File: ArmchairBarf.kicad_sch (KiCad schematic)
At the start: 12 parts, among them J1 Conn_01x03_Socket, U1 WS2812-2020, U2 WS2812-2020, U3 WS2812-2020, U4 WS2812-2020, U5 WS2812-2020, U6 WS2812-2020, U7 WS2812-2020, U8 WS2812-2020, U9 WS2812-2020

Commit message: Cleaned up and made proper connections and repinned to hartk's suggestions
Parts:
- added C2, C3, C4: C, Capacitor_SMD:C_0402_1005Metric, symbol Device:C
- added J2: Conn_01x03_Socket, Connector_JST:JST_PH_B3B-PH-K_1x03_P2.00mm_Vertical, symbol Connector:Conn_01x03_Socket
- added U10, U11, U12: WS2812-2020, LED_WS2812-2020, symbol WS2812-2020:WS2812-2020
- J1: footprint (none) -> Connector_JST:JST_PH_B3B-PH-K_1x03_P2.00mm_Vertical
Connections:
- net at U9.1 (DO): now also U10.3 (DI)
- net GND: now reaches C1.2, U1.2 (GND), U2.2 (GND), U3.2 (GND), U4.2 (GND), U5.2 (GND), U6.2 (GND), U7.2 (GND), U8.2 (GND), U9.2 (GND)
- net GND: now also J1.2 (Pin_2), C2.2, C3.2, C4.2, J2.2 (Pin_2), U10.2 (GND), U11.2 (GND), U12.2 (GND); no longer J1.1 (Pin_1)
- net +5V: now reaches C1.1, J1.3 (Pin_3), U1.4 (VDD), U2.4 (VDD), U3.4 (VDD), U4.4 (VDD), U5.4 (VDD), U6.4 (VDD), U7.4 (VDD), U8.4 (VDD), U9.4 (VDD)
- net +5V: now also C2.1, C3.1, C4.1, J2.3 (Pin_3), U10.4 (VDD), U11.4 (VDD), U12.4 (VDD)
- net at R1.1: now also J1.1 (Pin_1); no longer J1.2 (Pin_2)
- new net: J2.1 (Pin_1), U12.1 (DO)
- new net: U10.1 (DO), U11.3 (DI)
- new net: U11.1 (DO), U12.3 (DI)

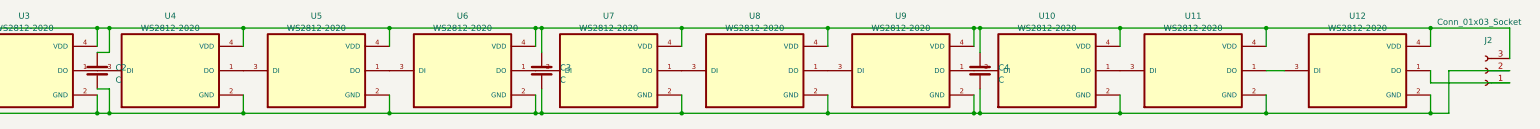
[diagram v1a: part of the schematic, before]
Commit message: Redesigned for Whopping's Rainbow Barf form factor.
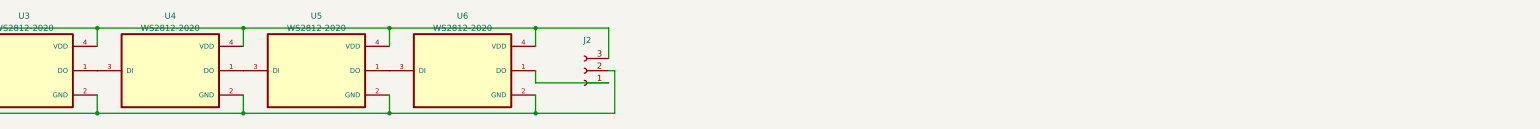
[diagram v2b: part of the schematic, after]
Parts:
- removed C2, C3, C4: C, Capacitor_SMD:C_0402_1005Metric, symbol Device:C
- removed U10, U11, U12, U7, U8, U9: WS2812-2020, LED_WS2812-2020, symbol WS2812-2020:WS2812-2020
- J1, J2: footprint Connector_JST:JST_PH_B3B-PH-K_1x03_P2.00mm_Vertical -> Connector_Wire:SolderWire-0.1sqmm_1x03_P3.6mm_D0.4mm_OD1mm
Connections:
- net at J2.1 (Pin_1): now also U6.1 (DO)
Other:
- moved on the sheet: J2
